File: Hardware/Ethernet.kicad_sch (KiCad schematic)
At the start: 31 parts, among them J5 MagJack_PoE, U4 KSZ8041NL/I

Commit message: More WIP
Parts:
- renumbered TP_VDDA1 to TP_VDDA_1
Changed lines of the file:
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@@
 		(dnp no)
 		(fields_autoplaced yes)
-		(property "Reference" "TP_VDDA1"
+		(property "Reference" "TP_VDDA_1"
 			(at 173.99 64.7699 90)
 			(effects
@@
 			(project "SparkFun_RTK_mosaic-T"
 				(path "/e3dd3ae4-244d-4cba-9cca-5d2abf83f29a/c43afff9-f83a-4a8d-a24d-a11c71953b08"
-					(reference "TP_VDDA1")
+					(reference "TP_VDDA_1")
 					(unit 1)
 				)

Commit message: More WIP
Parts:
- renumbered JP_SPEED1 to JP12, JP_LINK1 to JP13, TP_VDDA_1 to TP23
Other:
- moved on the sheet: JP12, JP13, R17, R18
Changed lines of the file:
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@@
 	(wire
 		(pts
-			(xy 66.04 78.74) (xy 68.58 78.74)
+			(xy 66.04 78.74) (xy 69.85 78.74)
 		)
 		(stroke
@@
 	(wire
 		(pts
-			(xy 86.36 83.82) (xy 87.63 83.82)
+			(xy 87.63 83.82) (xy 88.9 83.82)
 		)
 		(stroke
@@
 	(wire
 		(pts
-			(xy 76.2 83.82) (xy 78.74 83.82)
+			(xy 77.47 83.82) (xy 80.01 83.82)
 		)
 		(stroke
@@
 	(wire
 		(pts
-			(xy 66.04 83.82) (xy 68.58 83.82)
+			(xy 66.04 83.82) (xy 69.85 83.82)
 		)
 		(stroke
@@
 	(wire
 		(pts
-			(xy 76.2 78.74) (xy 78.74 78.74)
+			(xy 77.47 78.74) (xy 80.01 78.74)
 		)
 		(stroke
@@
 	(wire
 		(pts
-			(xy 86.36 78.74) (xy 87.63 78.74)
+			(xy 87.63 78.74) (xy 88.9 78.74)
 		)
 		(stroke
@@
 	(global_label "LINK"
 		(shape input)
-		(at 87.63 83.82 0)
+		(at 88.9 83.82 0)
 		(fields_autoplaced yes)
 		(effects
@@
 		)
 		(property "Intersheetrefs" "${INTERSHEET_REFS}"
-			(at 94.8486 83.82 0)
+			(at 96.1186 83.82 0)
 			(effects
 				(font
@@
 	(global_label "SPEED"
 		(shape input)
-		(at 87.63 78.74 0)
+		(at 88.9 78.74 0)
 		(fields_autoplaced yes)
 		(effects
@@
 		)
 		(property "Intersheetrefs" "${INTERSHEET_REFS}"
-			(at 96.6627 78.74 0)
+			(at 97.9327 78.74 0)
 			(effects
 				(font
@@
 		(dnp no)
 		(fields_autoplaced yes)
-		(property "Reference" "TP_VDDA_1"
+		(property "Reference" "TP23"
 			(at 173.99 64.7699 90)
 			(effects
@@
 			(project "SparkFun_RTK_mosaic-T"
 				(path "/e3dd3ae4-244d-4cba-9cca-5d2abf83f29a/c43afff9-f83a-4a8d-a24d-a11c71953b08"
-					(reference "TP_VDDA_1")
+					(reference "TP23")
 					(unit 1)
 				)
@@
 	(symbol
 		(lib_id "SparkFun-Resistor:1k_0603")
-		(at 82.55 83.82 0)
+		(at 83.82 83.82 0)
 		(unit 1)
 		(exclude_from_sim no)
@@
 		(dnp no)
 		(property "Reference" "R18"
-			(at 81.28 81.28 0)
+			(at 82.55 81.28 0)
 			(effects
 				(font
@@
 		)
 		(property "Value" "1k"
-			(at 85.09 81.28 0)
+			(at 86.36 81.28 0)
 			(effects
 				(font
@@
 		)
 		(property "Footprint" "SparkFun-Resistor:R_0603_1608Metric"
-			(at 82.55 88.392 0)
+			(at 83.82 88.392 0)
 			(effects
 				(font
@@
 		)
 		(property "Datasheet" "https://www.vishay.com/docs/20035/dcrcwe3.pdf"
-			(at 81.28 92.71 0)
+			(at 82.55 92.71 0)
 			(effects
 				(font
@@
 		)
 		(property "Description" "Resistor"
-			(at 82.55 95.25 0)
+			(at 83.82 95.25 0)
 			(effects
 				(font
@@
 		)
 		(property "PROD_ID" "RES-07856"
-			(at 82.55 90.678 0)
+			(at 83.82 90.678 0)
 			(effects
 				(font
@@
 	(symbol
 		(lib_id "SparkFun-Jumper:SolderJumper_2_Bridged")
-		(at 72.39 83.82 0)
+		(at 73.66 83.82 0)
 		(unit 1)
 		(exclude_from_sim no)
@@
 		(on_board yes)
 		(dnp no)
-		(property "Reference" "JP_LINK1"
+		(property "Reference" "JP13"
 			(at 73.66 81.28 0)
 			(effects
@@
 		)
 		(property "Value" "~"
-			(at 72.39 81.28 0)
+			(at 73.66 90.17 0)
 			(effects
 				(font
@@
 		)
 		(property "Footprint" "SparkFun-Jumper:Jumper_2_NC_Trace"
-			(at 72.136 88.392 0)
+			(at 73.406 88.392 0)
 			(effects
 				(font
@@
 		)
 		(property "Datasheet" "~"
-			(at 72.39 91.44 0)
+			(at 73.66 91.44 0)
 			(effects
 				(font
@@
 		)
 		(property "Description" "Solder Jumper, 2-pole, closed/bridged"
-			(at 72.39 83.82 0)
+			(at 73.66 83.82 0)
 			(effects
 				(font
@@
 			(project "SparkFun_RTK_mosaic-T"
 				(path "/e3dd3ae4-244d-4cba-9cca-5d2abf83f29a/c43afff9-f83a-4a8d-a24d-a11c71953b08"
-					(reference "JP_LINK1")
+					(reference "JP13")
 					(unit 1)
 				)
@@
 	(symbol
 		(lib_id "SparkFun-Resistor:1k_0603")
-		(at 82.55 78.74 0)
+		(at 83.82 78.74 0)
 		(unit 1)
 		(exclude_from_sim no)
@@
 		(dnp no)
 		(property "Reference" "R17"
-			(at 81.28 76.2 0)
+			(at 82.55 76.2 0)
 			(effects
 				(font
@@
 		)
 		(property "Value" "1k"
-			(at 85.09 76.2 0)
+			(at 86.36 76.2 0)
 			(effects
 				(font
@@
 		)
 		(property "Footprint" "SparkFun-Resistor:R_0603_1608Metric"
-			(at 82.55 83.312 0)
+			(at 83.82 83.312 0)
 			(effects
 				(font
@@
 		)
 		(property "Datasheet" "https://www.vishay.com/docs/20035/dcrcwe3.pdf"
-			(at 81.28 87.63 0)
+			(at 82.55 87.63 0)
 			(effects
 				(font
@@
 		)
 		(property "Description" "Resistor"
-			(at 82.55 90.17 0)
+			(at 83.82 90.17 0)
 			(effects
 				(font
@@
 		)
 		(property "PROD_ID" "RES-07856"
-			(at 82.55 85.598 0)
+			(at 83.82 85.598 0)
 			(effects
 				(font
@@
 	(symbol
 		(lib_id "SparkFun-Jumper:SolderJumper_2_Bridged")
-		(at 72.39 78.74 0)
+		(at 73.66 78.74 0)
 		(unit 1)
 		(exclude_from_sim no)
@@
 		(on_board yes)
 		(dnp no)
-		(property "Reference" "JP_SPEED1"
+		(property "Reference" "JP12"
 			(at 73.66 76.2 0)
 			(effects
@@
 		)
 		(property "Value" "~"
-			(at 72.39 76.2 0)
+			(at 73.66 76.2 0)
 			(effects
 				(font
@@
 		)
 		(property "Footprint" "SparkFun-Jumper:Jumper_2_NC_Trace"
-			(at 72.136 83.312 0)
+			(at 73.406 83.312 0)
 			(effects
 				(font
@@
 		)
 		(property "Datasheet" "~"
-			(at 72.39 86.36 0)
+			(at 73.66 86.36 0)
 			(effects
 				(font
@@
 		)
 		(property "Description" "Solder Jumper, 2-pole, closed/bridged"
-			(at 72.39 78.74 0)
+			(at 73.66 78.74 0)
 			(effects
 				(font
@@
 			(project ""
 				(path "/e3dd3ae4-244d-4cba-9cca-5d2abf83f29a/c43afff9-f83a-4a8d-a24d-a11c71953b08"
-					(reference "JP_SPEED1")
+					(reference "JP12")
 					(unit 1)
 				)

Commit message: More WIP
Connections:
- net LINK: now also R34.2, U4.30 (LED0/NWAYEN); no longer R35.2, U4.31 (LED1/SPEED)
- net SPEED: now also R35.2, U4.31 (LED1/SPEED); no longer R34.2, U4.30 (LED0/NWAYEN)
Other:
- note added: "50MHz"

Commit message: Routing WIP
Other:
- note added: "Ethernet Track Impedance: Differential Pair https://saturnpcb.com/saturn-pcb-toolkit/ Prepreg thickness: 8.3 mil (JLC7628). Er = 4.6 9.0 mil track with 11.0 mil gap (20 mil center to center) = 100 Ohms Each pair should match in length to better than 0.5mm"
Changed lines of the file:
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@@
+		)
+	)
+	(text "Ethernet Track Impedance: Differential Pair\nhttps://saturnpcb.com/saturn-pcb-toolkit/\nPrepreg thickness: 8.3 mil (JLC7628). Er = 4.6\n9.0 mil track with 11.0 mil gap (20 mil center to center) = 100 Ohms\nEach pair should match in length to better than 0.5mm"
+		(exclude_from_sim no)
+		(at 16.51 193.04 0)
+		(effects
+			(font
+				(size 1.27 1.27)
+			)
+			(justify left bottom)
 		)
 	)

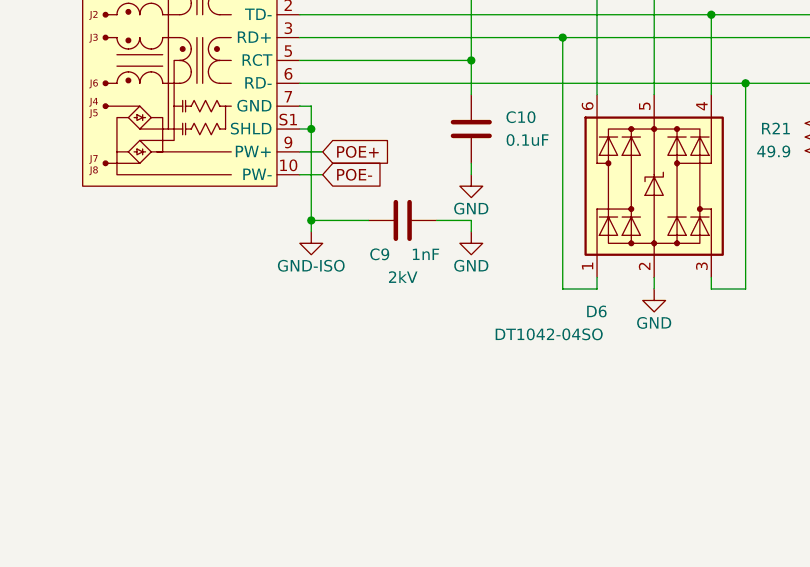
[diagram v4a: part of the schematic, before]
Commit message: Updates to match latest KiCad library
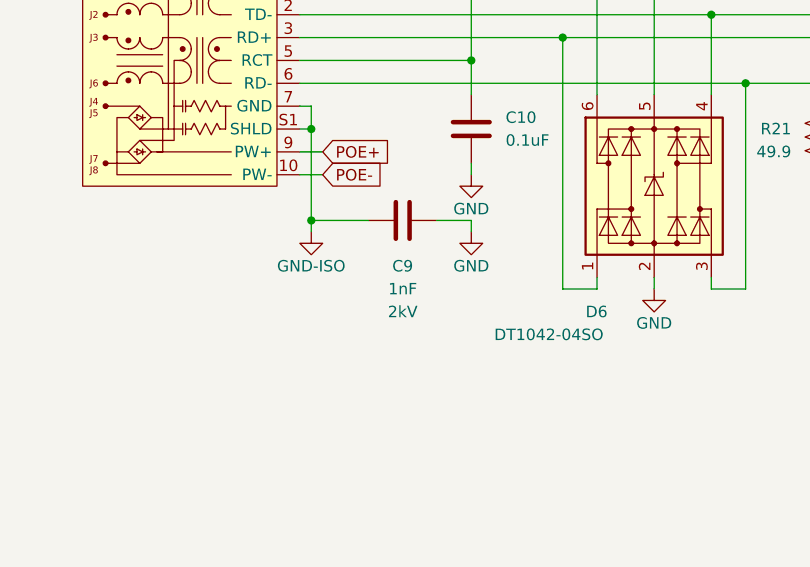
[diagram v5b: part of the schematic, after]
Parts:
- C9: symbol SparkFun-Capacitor:1nF_1206V_2kV_10% -> SparkFun-Capacitor:1.0nF_1206V_2kV_10%
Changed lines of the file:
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@@
 	)
 	(symbol
-		(lib_id "SparkFun-Capacitor:1nF_1206V_2kV_10%")
+		(lib_id "SparkFun-Capacitor:1.0nF_1206V_2kV_10%")
 		(at 77.47 114.3 90)
 		(mirror x)
@@
 		(on_board yes)
 		(dnp no)
+		(fields_autoplaced yes)
 		(property "Reference" "C9"
-			(at 74.93 118.11 90)
+			(at 77.47 119.38 90)
 			(effects
 				(font
@@
 		)
 		(property "Value" "1nF"
-			(at 80.01 118.11 90)
+			(at 77.47 121.92 90)
 			(effects
 				(font
@@
 		)
 		(property "Voltage" "2kV"
-			(at 77.47 120.65 90)
+			(at 77.47 124.46 90)
 			(effects
 				(font
@@
 		)
 		(property "Tolerance" "10%"
-			(at 80.01 120.65 90)
+			(at 77.47 127 90)
 			(effects
 				(font
